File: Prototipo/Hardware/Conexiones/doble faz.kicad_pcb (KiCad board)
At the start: 2 copper layers, 50 x 100 mm, 6 parts, among them J1 Raspberry Pi, J2 Termocupla, J3 Frente, J4 PT100, J6 Rele

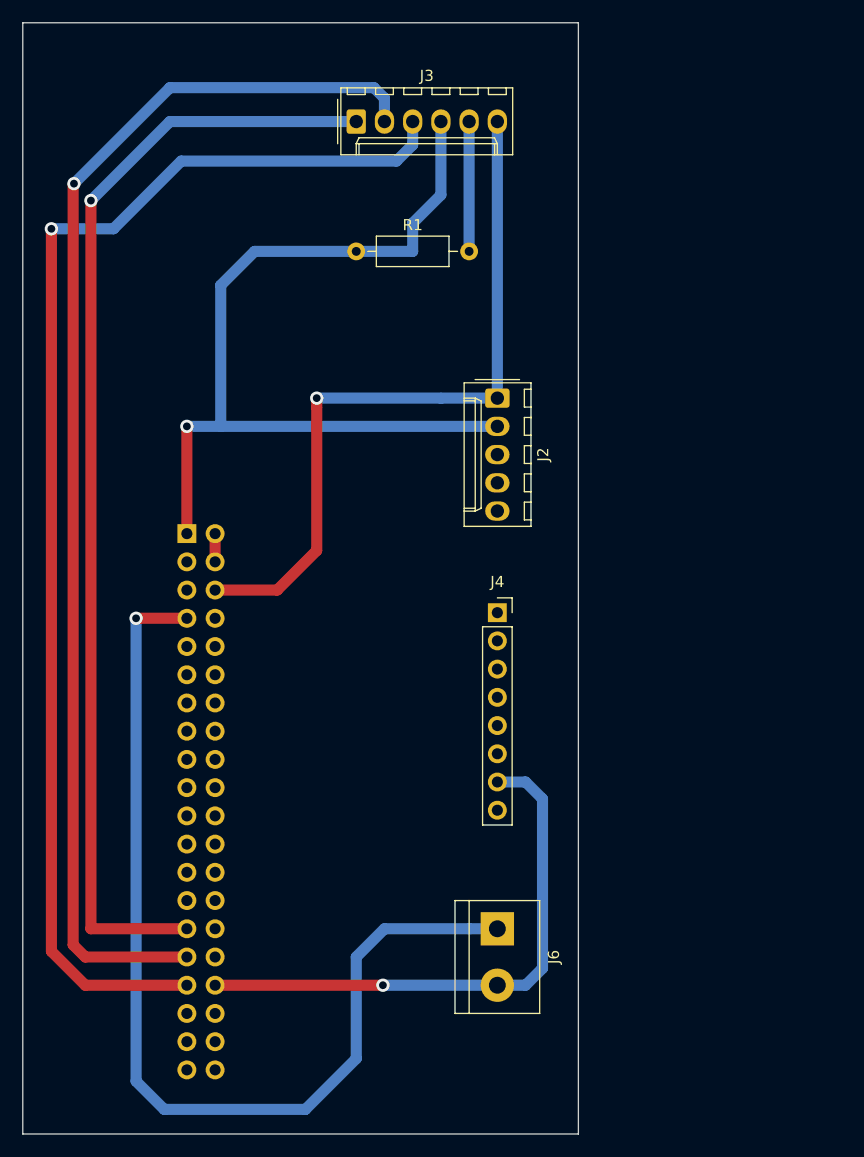
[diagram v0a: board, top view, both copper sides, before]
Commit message: placa doble faz lista
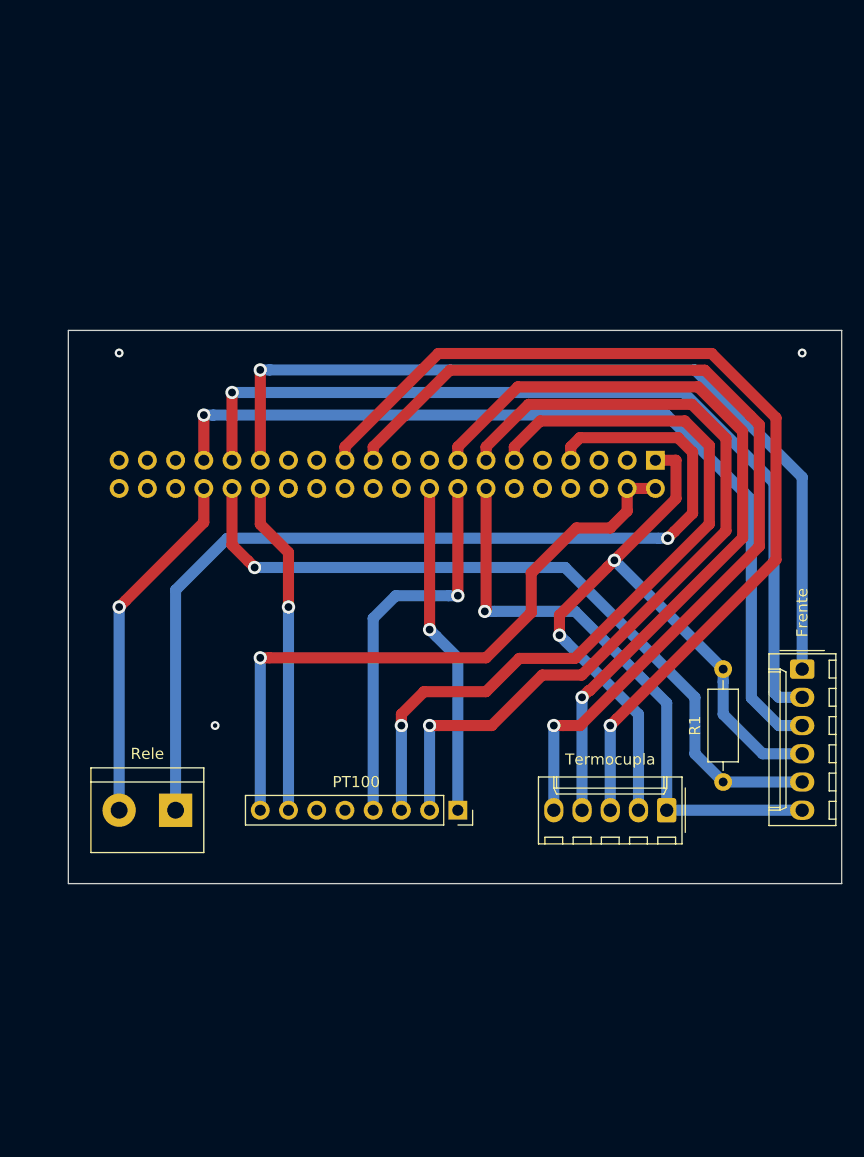
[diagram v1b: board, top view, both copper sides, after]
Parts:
- removed J2: Termocupla, Connector_Molex:Molex_KK-254_AE-6410-05A_1x05_P2.54mm_Vertical
- removed J3: Frente, Connector_Molex:Molex_KK-254_AE-6410-06A_1x06_P2.54mm_Vertical
- removed J6: Rele, TerminalBlock:TerminalBlock_bornier-2_P5.08mm
- added Frente: Frente, Connector_Molex:Molex_KK-254_AE-6410-06A_1x06_P2.54mm_Vertical, F.Cu at (167.6, 105.7)
- added Rele: Rele, TerminalBlock:TerminalBlock_bornier-2_P5.08mm, F.Cu at (111.3, 118.4)
- added Termocupla: Termocupla, Connector_Molex:Molex_KK-254_AE-6410-05A_1x05_P2.54mm_Vertical, F.Cu at (155.4, 118.4)
- moved R1 50.0 mm to (160.5, 105.7), turned to 270 degrees
- moved J1 42.7 mm to (154.4, 86.9), turned to 90 degrees
- moved PT100 18.1 mm to (136.7, 118.4), turned to 270 degrees
- renumbered J4 to PT100
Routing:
- net /t_clk: track 0.00 -> 87.4 mm, vias 0 -> 1
- net /t_miso: track 0.00 -> 84.6 mm, vias 0 -> 1
- net /p_cs: track 0.00 -> 75.5 mm, vias 0 -> 1
- net /p_clk: track 0.00 -> 71.1 mm, vias 0 -> 1
- net /t_cs: track 0.00 -> 70.9 mm, vias 0 -> 1
- net /b_out: track 11.7 -> 68.2 mm, vias 0 -> 1
- net /5v: track 2.54 -> 58.9 mm, vias 0 -> 1
- net /led_3: track 116.2 -> 79.9 mm
- net /p_mosi: track 0.00 -> 35.4 mm, vias 0 -> 1
- net /led_2: track 113.2 -> 79.8 mm
- net /p_miso: track 0.00 -> 30.0 mm, vias 0 -> 1
- net /led_1: track 101.0 -> 78.2 mm
- net /3v3: track 81.6 -> 67.1 mm, vias 1 -> 2
- net /r_out: track 91.9 -> 87.8 mm
- net GND: track 115.5 -> 114.9 mm, vias 2 -> 3
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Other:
- board size 50 x 100 mm -> 69.6 x 49.8 mm
